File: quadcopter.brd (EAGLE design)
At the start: 127.2 x 127.2 mm, 77 parts, among them J1 AVR_SPI_PRG_6NS, J3 HEADER-0.1IN-2POS-FEMALE, J4 HEADER-0.1IN-2POS-FEMALE, J5 HEADER-0.1IN-2POS-FEMALE, J6 HEADER-0.1IN-2POS-FEMALE, J8 HEADER-0.1IN-2POS-FEMALE, SW1 PUSHBUTTON_SMD-VERTICAL, SW2 PUSHBUTTON_SMD-VERTICAL, U1 ATMEGA128RFA1

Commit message: swaped motor 2 and 4
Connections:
- net M2_CTL: now also U1.30; no longer U1.19
- net M4_CTL: now also U1.19; no longer U1.30
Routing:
- net M4_CTL: track 2.32 -> 0.00 mm
- net M2_CTL: track 0.00 -> 2.32 mm
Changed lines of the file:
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@@
 <contactref element="R6" pad="1"/>
 <contactref element="C21" pad="1"/>
-<contactref element="U1" pad="30"/>
 <contactref element="J6" pad="2"/>
-<wire x1="-4.881" y1="11.25" x2="-7.2" y2="11.25" width="0.2032" layer="1"/>
-<wire x1="-35.3671375" y1="34.3671375" x2="-36.8247125" y2="32.8247125" width="0" layer="19" extent="1-1"/>
-<wire x1="-23.46" y1="26" x2="-35.3671375" y2="34.3671375" width="0" layer="19" extent="1-1"/>
-<wire x1="-7.2" y1="11.25" x2="-23.46" y2="26" width="0" layer="19" extent="1-1"/>
+<contactref element="U1" pad="19"/>
+<wire x1="-23.46" y1="26" x2="-4.881" y2="16.75" width="0" layer="19" extent="1-1"/>
+<wire x1="-35.3671375" y1="34.3671375" x2="-23.46" y2="26" width="0" layer="19" extent="1-1"/>
+<wire x1="-36.8247125" y1="32.8247125" x2="-35.3671375" y2="34.3671375" width="0" layer="19" extent="1-1"/>
 </signal>
 <signal name="N$8">
@@
 <contactref element="R8" pad="1"/>
 <contactref element="C19" pad="1"/>
-<contactref element="U1" pad="19"/>
 <contactref element="J4" pad="2"/>
+<contactref element="U1" pad="30"/>
+<wire x1="-4.881" y1="11.25" x2="-7.2" y2="11.25" width="0.2032" layer="1"/>
 <wire x1="-39.632859375" y1="-40.632859375" x2="-38.175284375" y2="-42.175284375" width="0" layer="19" extent="1-1"/>
 <wire x1="-23.46" y1="-26" x2="-39.632859375" y2="-40.632859375" width="0" layer="19" extent="1-1"/>
-<wire x1="-4.881" y1="16.75" x2="-23.46" y2="-26" width="0" layer="19" extent="1-1"/>
+<wire x1="-7.2" y1="11.25" x2="-23.46" y2="-26" width="0" layer="19" extent="1-1"/>
 </signal>
 <signal name="N$13">

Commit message: passing parts of drc
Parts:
- moved C5 1.55 mm to (-19.0, 25.8), turned to 0 degrees
- moved C16 1.52 mm to (-25.0, -5.48)
- moved R3 1.00 mm to (-20.0, 23.0)
- moved R13 0.76 mm to (15.8, 23.0)
- moved C23 0.57 mm to (15.3, 15.5)
- moved C9 0.51 mm to (-37.0, 41.5)
- moved U$8 0.51 mm to (-29.5, -10.0)
- moved Y1 0.51 mm to (11.0, 16.5)
- moved C22 0.36 mm to (15.3, 19.3)
- moved R12 0.36 mm to (11.7, 23.3)
- moved C10 0.36 mm to (40.8, 36.7)
- moved C2 0.25 mm to (-3.49, 23.8)
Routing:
- net V_BAT: track 19.6 -> 14.8 mm
- net RESET: track 7.20 -> 6.05 mm
- net GND: track 31.9 -> 32.4 mm

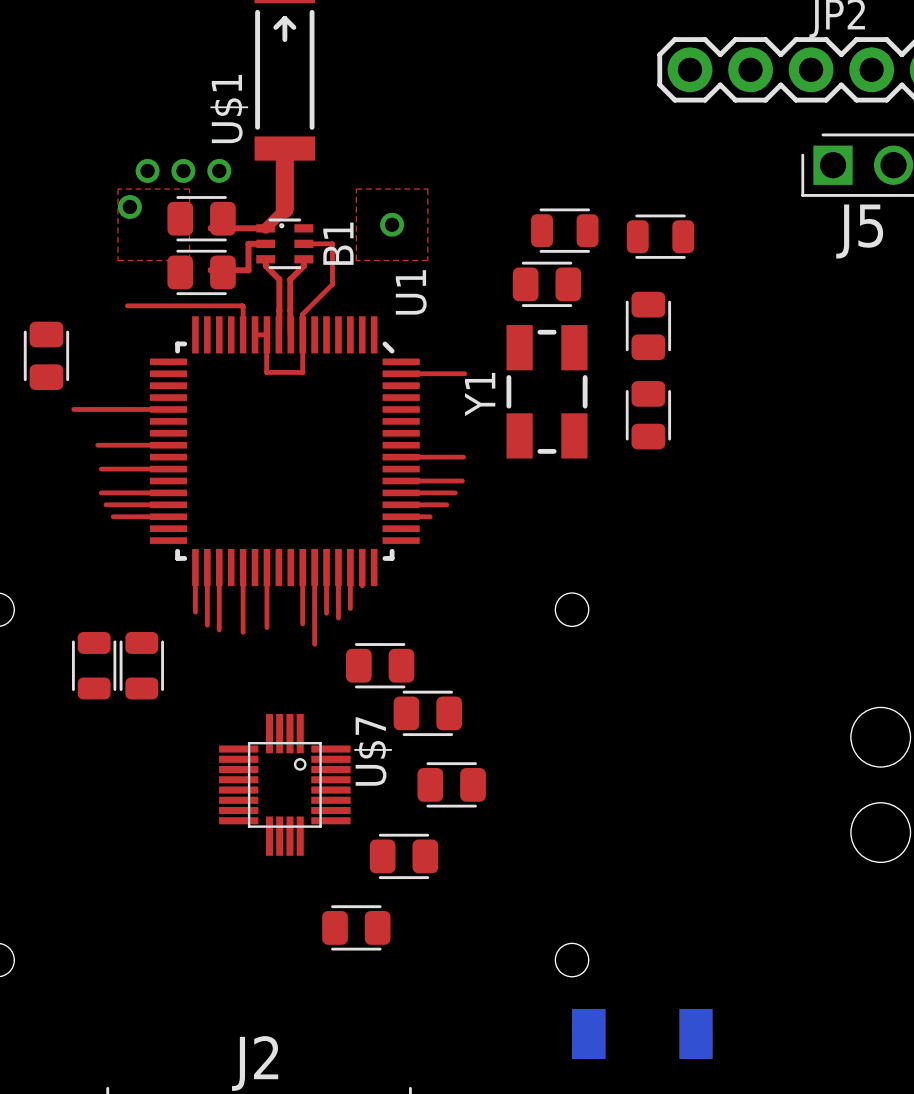
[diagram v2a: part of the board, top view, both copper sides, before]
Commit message: Made tkeepouts stricter on imu, laid out components out nicer
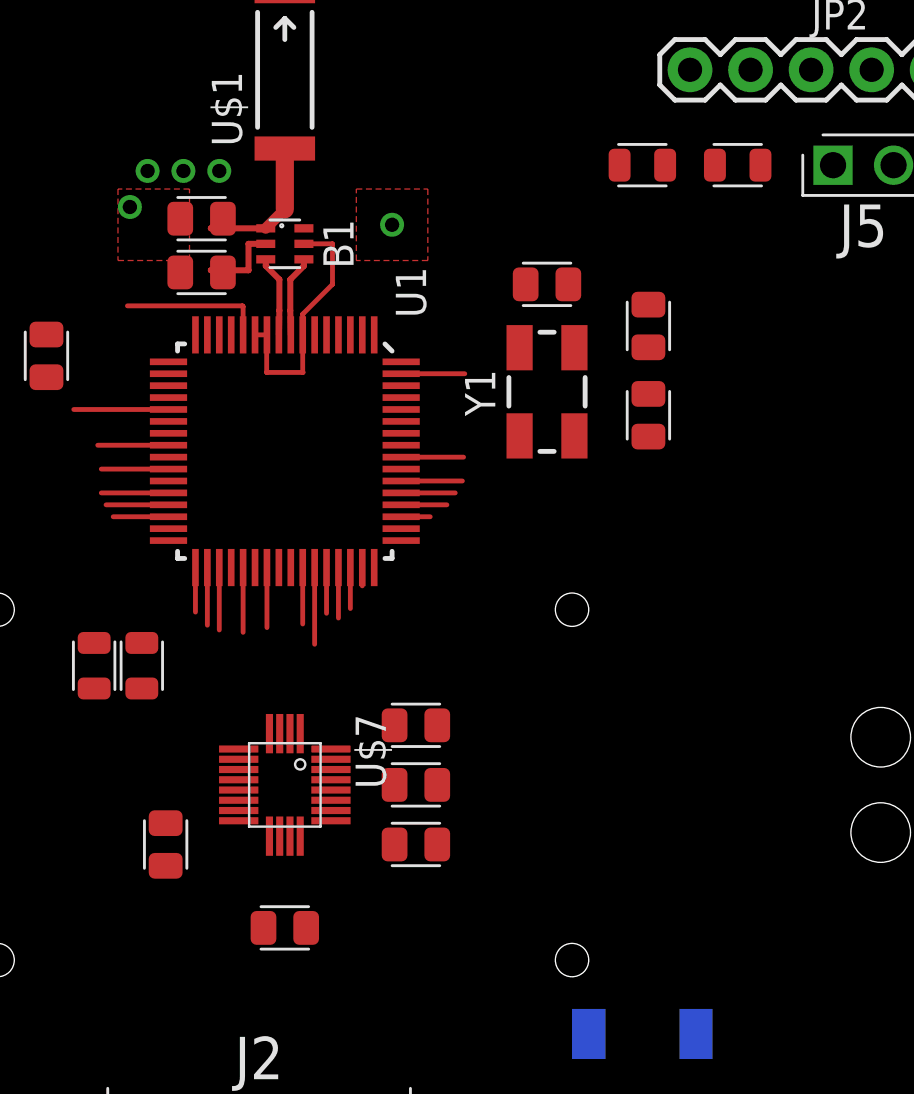
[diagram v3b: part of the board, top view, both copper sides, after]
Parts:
- moved C6 12.3 mm to (-5.00, -2.50), turned to 270 degrees
- moved R13 4.41 mm to (19.0, 26.0)
- moved R12 4.26 mm to (15.0, 26.0)
- moved C8 3.04 mm to (5.50, 0.00)
- moved C13 3.00 mm to (0.00, -6.00)
- moved C7 2.92 mm to (5.50, 2.50)
- moved C14 0.71 mm to (5.50, -2.50), turned to 180 degrees

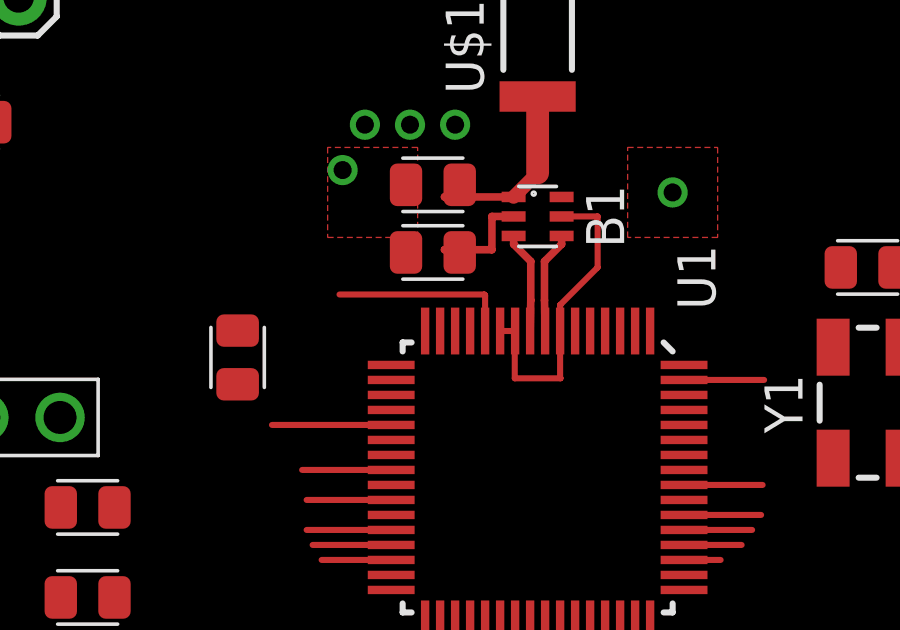
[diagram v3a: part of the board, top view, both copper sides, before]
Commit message: Made cutout in pour for imu
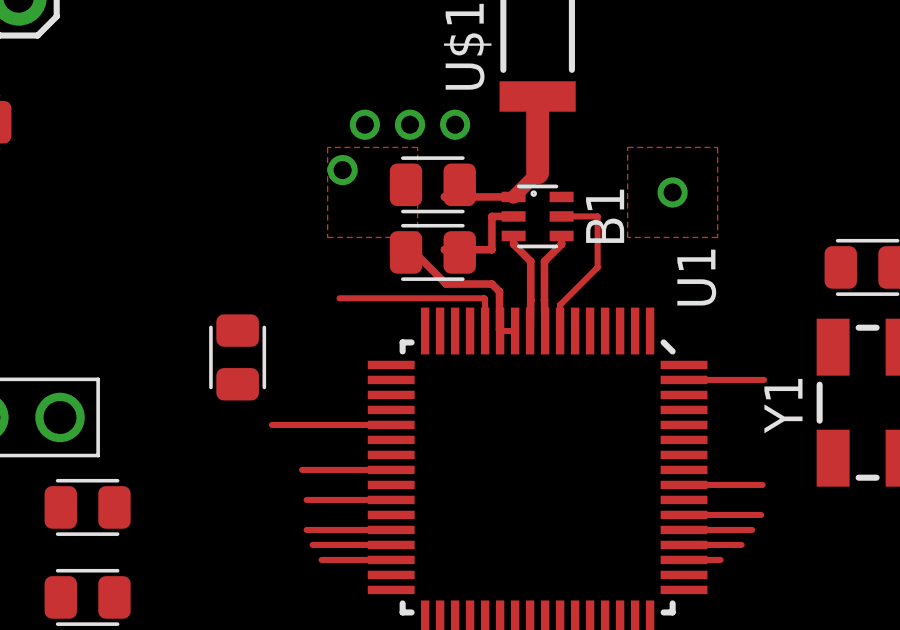
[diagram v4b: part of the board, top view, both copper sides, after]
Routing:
- net GND: track 32.4 -> 32.7 mm, vias 0 -> 5
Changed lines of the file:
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@@
 <setting verticaltext="up"/>
 </settings>
-<grid distance="0.5" unitdist="mm" unit="mm" style="lines" multiple="1" display="yes" altdistance="0.025" altunitdist="inch" altunit="inch"/>
+<grid distance="5" unitdist="mil" unit="mil" style="lines" multiple="1" display="yes" altdistance="0.025" altunitdist="inch" altunit="inch"/>
 <layers>
 <layer number="1" name="Top" color="4" fill="1" visible="yes" active="yes"/>
-<layer number="2" name="Route2" color="1" fill="3" visible="yes" active="yes"/>
+<layer number="2" name="Route2" color="1" fill="3" visible="no" active="yes"/>
 <layer number="3" name="Route3" color="4" fill="3" visible="no" active="no"/>
 <layer number="4" name="Route4" color="1" fill="4" visible="no" active="no"/>
@@
 <layer number="13" name="Route13" color="4" fill="5" visible="no" active="no"/>
 <layer number="14" name="Route14" color="1" fill="6" visible="no" active="no"/>
-<layer number="15" name="Route15" color="4" fill="6" visible="yes" active="yes"/>
+<layer number="15" name="Route15" color="4" fill="6" visible="no" active="yes"/>
 <layer number="16" name="Bottom" color="1" fill="1" visible="yes" active="yes"/>
 <layer number="17" name="Pads" color="2" fill="1" visible="yes" active="yes"/>
@@
 <vertex x="7" y="24"/>
 <vertex x="-8" y="24"/>
+</polygon>
+<polygon width="0.4064" layer="43">
+<vertex x="-4.5" y="18.5"/>
+<vertex x="4.5" y="18.5"/>
+<vertex x="4.5" y="9.5"/>
+<vertex x="-4.5" y="9.5"/>
 </polygon>
 </plain>
@@
 <vertex x="-19" y="-9"/>
 <vertex x="-19" y="23"/>
+<vertex x="-10" y="23"/>
+<vertex x="-4.5" y="7.5"/>
+<vertex x="-4.5" y="-4.5"/>
+<vertex x="5" y="-4.5"/>
+<vertex x="5" y="7.5"/>
+<vertex x="10" y="23"/>
 <vertex x="18" y="23"/>
-<vertex x="18" y="22"/>
 <vertex x="18" y="-23"/>
 <vertex x="-19" y="-23"/>
@@
 <wire x1="2" y1="21" x2="2" y2="22.7" width="0.2032" layer="1"/>
 <wire x1="-1.25" y1="18.881" x2="-0.75" y2="18.881" width="0.2032" layer="1"/>
-<wire x1="0.75" y1="18.881" x2="0.75" y2="17.316" width="0.2032" layer="1"/>
-<wire x1="0.75" y1="17.316" x2="0.762" y2="17.304" width="0.2032" layer="1"/>
-<wire x1="0.762" y1="17.304" x2="-0.762" y2="17.304" width="0.2032" layer="1"/>
-<wire x1="-0.762" y1="17.304" x2="-0.762" y2="18.869" width="0.2032" layer="1"/>
 <wire x1="-0.762" y1="18.869" x2="-0.75" y2="18.881" width="0.2032" layer="1"/>
 <wire x1="-4.881" y1="14.25" x2="-7.85" y2="14.25" width="0.2032" layer="1"/>
@@
 <wire x1="-2.75" y1="9.119" x2="-2.75" y2="6.5" width="0.2032" layer="1"/>
 <wire x1="-3.75" y1="9.119" x2="-3.75" y2="7.25" width="0.2032" layer="1"/>
+<via x="4.5" y="23.5" extent="1-16" drill="0.6" shape="square"/>
+<via x="-6.5" y="24.246" extent="1-16" drill="0.6" shape="square"/>
+<via x="-5.758" y="25.758" extent="1-16" drill="0.6" shape="square"/>
+<via x="-4.254" y="25.758" extent="1-16" drill="0.6" shape="square"/>
+<via x="-2.75" y="25.758" extent="1-16" drill="0.6" shape="square"/>
+<wire x1="-4.064" y1="21.463" x2="-4.318" y2="21.463" width="0.254" layer="1"/>
+<wire x1="-3.048" y1="20.447" x2="-4.064" y2="21.463" width="0.254" layer="1"/>
+<wire x1="-1.524" y1="20.447" x2="-3.048" y2="20.447" width="0.254" layer="1"/>
+<wire x1="-1.27" y1="20.193" x2="-1.524" y2="20.447" width="0.254" layer="1"/>
+<wire x1="-1.27" y1="18.923" x2="-1.27" y2="20.193" width="0.254" layer="1"/>
+<wire x1="-4.318" y1="21.463" x2="-4.387" y2="21.5" width="0.254" layer="1"/>
+<wire x1="-1.27" y1="18.923" x2="-1.25" y2="18.881" width="0.254" layer="1"/>
 <wire x1="19.955" y1="26" x2="29.7" y2="30" width="0" layer="19" extent="1-1"/>
 <wire x1="15.254" y1="20.149" x2="19.955" y2="26" width="0" layer="19" extent="1-1"/>
 <wire x1="15.254" y1="16.403" x2="15.254" y2="20.149" width="0" layer="19" extent="1-1"/>
 <wire x1="10.105" y1="21" x2="15.254" y2="20.149" width="0" layer="19" extent="1-1"/>
-<wire x1="4.881" y1="16.25" x2="10.105" y2="21" width="0" layer="19" extent="1-1"/>
+<wire x1="4.5" y1="23.5" x2="10.105" y2="21" width="0" layer="19" extent="1-1"/>
+<wire x1="2" y1="22.7" x2="4.5" y2="23.5" width="0" layer="19" extent="1-1"/>
+<wire x1="-0.75" y1="18.881" x2="0.75" y2="18.881" width="0" layer="19" extent="1-1"/>
+<wire x1="-4.387" y1="23.754" x2="-4.387" y2="21.5" width="0" layer="19" extent="1-1"/>
+<wire x1="-4.254" y1="25.758" x2="-4.387" y2="23.754" width="0" layer="19" extent="1-1"/>
+<wire x1="-2.75" y1="25.758" x2="-4.254" y2="25.758" width="0" layer="19" extent="1-1"/>
+<wire x1="-5.758" y1="25.758" x2="-4.254" y2="25.758" width="0" layer="19" extent="1-1"/>
+<wire x1="-6.5" y1="24.246" x2="-5.758" y2="25.758" width="0" layer="19" extent="1-1"/>
+<wire x1="-4.881" y1="16.25" x2="-1.27" y2="18.923" width="0" layer="19" extent="1-1"/>
+<wire x1="-4.881" y1="14.25" x2="-4.881" y2="16.25" width="0" layer="19" extent="1-1"/>
+<wire x1="-10" y1="17.105" x2="-7.85" y2="14.25" width="0" layer="19" extent="1-1"/>
+<wire x1="4.881" y1="16.25" x2="0.75" y2="18.881" width="0" layer="19" extent="1-1"/>
 <wire x1="4.881" y1="14.75" x2="4.881" y2="16.25" width="0" layer="19" extent="1-1"/>
 <wire x1="4.881" y1="13.25" x2="4.881" y2="14.75" width="0" layer="19" extent="1-1"/>
-<wire x1="0.75" y1="17.316" x2="4.881" y2="16.25" width="0" layer="19" extent="1-1"/>
-<wire x1="-4.387" y1="21.5" x2="-1.25" y2="18.881" width="0" layer="19" extent="1-1"/>
-<wire x1="-4.387" y1="23.754" x2="-4.387" y2="21.5" width="0" layer="19" extent="1-1"/>
-<wire x1="-4.881" y1="16.25" x2="-0.762" y2="17.304" width="0" layer="19" extent="1-1"/>
-<wire x1="-4.881" y1="14.25" x2="-4.881" y2="16.25" width="0" layer="19" extent="1-1"/>
-<wire x1="-10" y1="17.105" x2="-7.85" y2="14.25" width="0" layer="19" extent="1-1"/>
 <wire x1="2.25" y1="9.119" x2="4.881" y2="13.25" width="0" layer="19" extent="1-1"/>
 <wire x1="-2.75" y1="9.119" x2="2.25" y2="9.119" width="0" layer="19" extent="1-1"/>
@@
 <wire x1="-25.895" y1="-5.476" x2="-26" y2="-7" width="0" layer="19" extent="1-1"/>
 <wire x1="15" y1="-15.955" x2="4" y2="-18.9" width="0" layer="19" extent="1-1"/>
-<wire x1="-17.3" y1="30" x2="-18.46" y2="16" width="0" layer="19" extent="1-1"/>
+<wire x1="-17.3" y1="30" x2="-6.5" y2="24.246" width="0" layer="19" extent="1-1"/>
 </signal>
 <signal name="RFP">
@@
 <vertex x="-19" y="23"/>
 <vertex x="-10" y="23"/>
-<vertex x="-10" y="20"/>
-<vertex x="10" y="20"/>
+<vertex x="-4.5" y="7.5"/>
+<vertex x="-4.5" y="-4"/>
+<vertex x="-3.5" y="-4"/>
+<vertex x="4" y="-4.5"/>
+<vertex x="5" y="-4.5"/>
+<vertex x="5" y="7.5"/>
 <vertex x="10" y="23"/>
 <vertex x="18" y="23"/>
@@
 <contactref element="J1" pad="5"/>
 <contactref element="C5" pad="1"/>
-<wire x1="-1.75" y1="18.881" x2="-1.75" y2="20.07" width="0.2032" layer="1"/>
-<wire x1="-1.75" y1="20.07" x2="-1.778" y2="20.098" width="0.2032" layer="1"/>
-<wire x1="-1.778" y1="20.098" x2="-6.604" y2="20.098" width="0.2032" layer="1"/>
+<wire x1="-1.75" y1="18.881" x2="-1.75" y2="19.943" width="0.2032" layer="1"/>
+<wire x1="-1.75" y1="19.943" x2="-1.778" y2="19.971" width="0.2032" layer="1"/>
+<wire x1="-1.778" y1="19.971" x2="-6.604" y2="19.971" width="0.2032" layer="1"/>
 <wire x1="-20" y1="23.955" x2="-23.73" y2="10.54" width="0" layer="19" extent="1-1"/>
 <wire x1="-19.869" y1="25.842" x2="-20" y2="23.955" width="0" layer="19" extent="1-1"/>
-<wire x1="-6.604" y1="20.098" x2="-20" y2="23.955" width="0" layer="19" extent="1-1"/>
+<wire x1="-6.604" y1="19.971" x2="-20" y2="23.955" width="0" layer="19" extent="1-1"/>
 </signal>
 <signal name="BAT_GND" class="1">
@@
 </polygon>
 </signal>
-<signal name="N$22">
-<via x="-2.75" y="25.758" extent="1-16" drill="0.6" shape="square"/>
-</signal>
-<signal name="N$23">
-<via x="-4.254" y="25.758" extent="1-16" drill="0.6" shape="square"/>
-</signal>
-<signal name="N$24">
-<via x="-5.758" y="25.758" extent="1-16" drill="0.6" shape="square"/>
-</signal>
-<signal name="N$25">
-<via x="-6.5" y="24.246" extent="1-16" drill="0.6" shape="square"/>
-</signal>
-<signal name="N$26">
-<via x="4.5" y="23.5" extent="1-16" drill="0.6" shape="square"/>
-</signal>
 </signals>

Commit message: fixed pwm filters
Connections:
- net M1_CTL: no longer C18.1
- net M2_CTL: no longer C19.1
- net M3_CTL: no longer C20.1
- net M4_CTL: no longer C21.1
- net N$11: now also C19.1
- net N$12: now also C21.1; no longer R7.1
- net N$13: now also C18.1
- net N$8: now also C20.1
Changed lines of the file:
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@@
 </signal>
 <signal name="M4_CTL">
-<contactref element="R6" pad="1"/>
-<contactref element="C21" pad="1"/>
 <contactref element="J6" pad="2"/>
 <contactref element="U1" pad="19"/>
+<contactref element="R6" pad="1"/>
 <wire x1="-23.46" y1="26" x2="-4.881" y2="16.75" width="0" layer="19" extent="1-1"/>
-<wire x1="-35.3671375" y1="34.3671375" x2="-23.46" y2="26" width="0" layer="19" extent="1-1"/>
-<wire x1="-36.8247125" y1="32.8247125" x2="-35.3671375" y2="34.3671375" width="0" layer="19" extent="1-1"/>
+<wire x1="-36.8247125" y1="32.8247125" x2="-23.46" y2="26" width="0" layer="19" extent="1-1"/>
 </signal>
 <signal name="N$8">
@@
 <contactref element="R4" pad="2"/>
 <contactref element="U$12" pad="G"/>
+<contactref element="C20" pad="1"/>
 <wire x1="33.8247125" y1="37.675284375" x2="36.34615" y2="41.54320625" width="0" layer="19" extent="1-1"/>
 <wire x1="32.675284375" y1="36.175284375" x2="33.8247125" y2="37.675284375" width="0" layer="19" extent="1-1"/>
+<wire x1="32.8671375" y1="33.3671375" x2="32.675284375" y2="36.175284375" width="0" layer="19" extent="1-1"/>
 </signal>
 <signal name="M3_CTL">
-<contactref element="R4" pad="1"/>
-<contactref element="C20" pad="1"/>
 <contactref element="U1" pad="29"/>
 <contactref element="J5" pad="2"/>
 <wire x1="-4.881" y1="11.75" x2="-7.5" y2="11.75" width="0.2032" layer="1"/>
-<wire x1="32.8671375" y1="33.3671375" x2="31.3247125" y2="34.8247125" width="0" layer="19" extent="1-1"/>
-<wire x1="25.54" y1="26" x2="32.8671375" y2="33.3671375" width="0" layer="19" extent="1-1"/>
+<contactref element="R4" pad="1"/>
+<wire x1="25.54" y1="26" x2="31.3247125" y2="34.8247125" width="0" layer="19" extent="1-1"/>
 <wire x1="-4.881" y1="11.75" x2="25.54" y2="26" width="0" layer="19" extent="1-1"/>
 </signal>
@@
 <contactref element="R8" pad="2"/>
 <contactref element="U$9" pad="G"/>
+<contactref element="C19" pad="1"/>
 <wire x1="-39.3247125" y1="-43.675284375" x2="-41.84615" y2="-46.54320625" width="0" layer="19" extent="1-1"/>
-<wire x1="-36.8247125" y1="-40.8247125" x2="-39.3247125" y2="-43.675284375" width="0" layer="19" extent="1-1"/>
+<wire x1="-39.632859375" y1="-40.632859375" x2="-39.3247125" y2="-43.675284375" width="0" layer="19" extent="1-1"/>
+<wire x1="-36.8247125" y1="-40.8247125" x2="-39.632859375" y2="-40.632859375" width="0" layer="19" extent="1-1"/>
 </signal>
 <signal name="M2_CTL">
-<contactref element="R8" pad="1"/>
-<contactref element="C19" pad="1"/>
 <contactref element="J4" pad="2"/>
 <contactref element="U1" pad="30"/>
 <wire x1="-4.881" y1="11.25" x2="-7.2" y2="11.25" width="0.2032" layer="1"/>
-<wire x1="-39.632859375" y1="-40.632859375" x2="-38.175284375" y2="-42.175284375" width="0" layer="19" extent="1-1"/>
-<wire x1="-23.46" y1="-26" x2="-39.632859375" y2="-40.632859375" width="0" layer="19" extent="1-1"/>
+<contactref element="R8" pad="1"/>
+<wire x1="-23.46" y1="-26" x2="-38.175284375" y2="-42.175284375" width="0" layer="19" extent="1-1"/>
 <wire x1="-7.2" y1="11.25" x2="-23.46" y2="-26" width="0" layer="19" extent="1-1"/>
 </signal>
@@
 <contactref element="R10" pad="2"/>
 <contactref element="U$11" pad="G"/>
+<contactref element="C18" pad="1"/>
 <wire x1="39.175284375" y1="-34.175284375" x2="40.675284375" y2="-35.3247125" width="0" layer="19" extent="1-1"/>
+<wire x1="36.3671375" y1="-34.3671375" x2="39.175284375" y2="-34.175284375" width="0" layer="19" extent="1-1"/>
 <wire x1="43.54320625" y1="-37.84615" x2="40.675284375" y2="-35.3247125" width="0" layer="19" extent="1-1"/>
 </signal>
 <signal name="M1_CTL">
-<contactref element="R10" pad="1"/>
-<contactref element="C18" pad="1"/>
 <contactref element="U1" pad="41"/>
 <contactref element="J3" pad="2"/>
+<contactref element="R10" pad="1"/>
 <wire x1="25.54" y1="-26" x2="0.25" y2="9.119" width="0" layer="19" extent="1-1"/>
-<wire x1="36.3671375" y1="-34.3671375" x2="25.54" y2="-26" width="0" layer="19" extent="1-1"/>
-<wire x1="37.8247125" y1="-32.8247125" x2="36.3671375" y2="-34.3671375" width="0" layer="19" extent="1-1"/>
+<wire x1="37.8247125" y1="-32.8247125" x2="25.54" y2="-26" width="0" layer="19" extent="1-1"/>
 </signal>
 <signal name="SCL">
@@
 <signal name="N$12">
 <contactref element="R6" pad="2"/>
-<contactref element="R7" pad="1"/>
 <contactref element="U$10" pad="G"/>
-<wire x1="-40.675284375" y1="36.3247125" x2="-38.175284375" y2="34.175284375" width="0" layer="19" extent="1-1"/>
-<wire x1="-43.54320625" y1="38.84615" x2="-40.675284375" y2="36.3247125" width="0" layer="19" extent="1-1"/>
+<contactref element="C21" pad="1"/>
+<wire x1="-35.3671375" y1="34.3671375" x2="-38.175284375" y2="34.175284375" width="0" layer="19" extent="1-1"/>
+<wire x1="-43.54320625" y1="38.84615" x2="-38.175284375" y2="34.175284375" width="0" layer="19" extent="1-1"/>
 </signal>
 <signal name="N$7">
